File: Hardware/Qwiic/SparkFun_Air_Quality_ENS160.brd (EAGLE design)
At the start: 25.4 x 25.4 mm, 49 parts, among them J1 QWIIC_RIGHT_ANGLE, J2 QWIIC_RIGHT_ANGLE, U1 AP2127K-1.8V

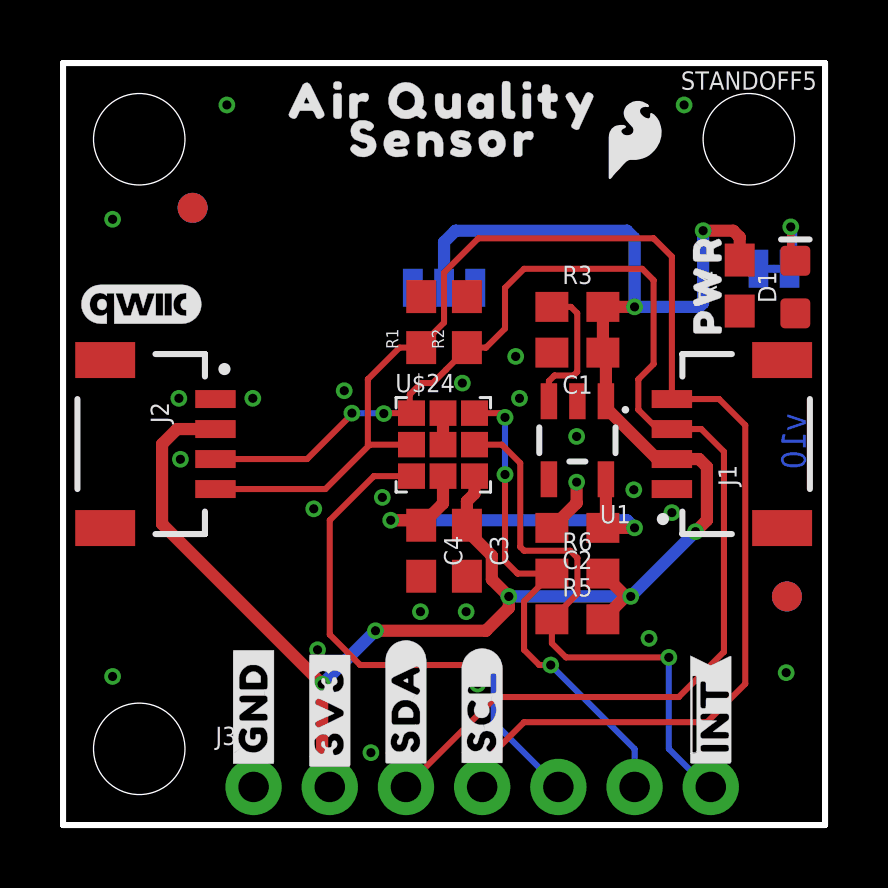
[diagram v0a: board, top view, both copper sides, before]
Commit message: Finishes routing, adds silk
* Updates ENS160 symbol to be smaller
* Adds "U" prefix to device
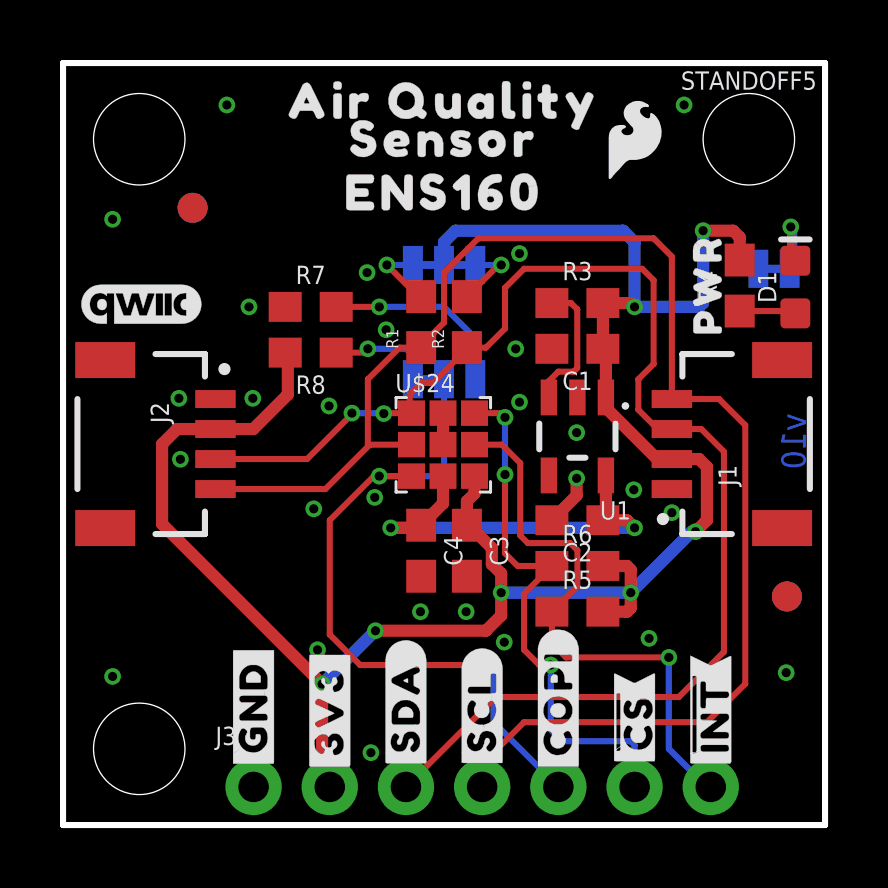
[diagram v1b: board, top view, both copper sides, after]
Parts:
- removed LOGO1: SPECIAL_INSTRUCTIONS-PRODUCTION, SparkFun-Aesthetics:PRODUCTION_INSTRUCTIONS
- added ADDR: JUMPER-SMT_3_1-NC_TRACE_SILK, SparkFun-Jumpers:SMT-JUMPER_3_1-NC_TRACE_SILK
- added R7, R8: 100k, SparkFun-Resistors:0603
- added U$14: (no value), top:#0X53#16019
- added U$15: (no value), top:#0X52#16019
- added U$23: (no value), top:#COPI#16020
- added U$26: (no value), bot:#COPI#441017
- added U$27: (no value), bot:##CS##441016
- added U$28, U$5: (no value), top:ENS16016
- added U$6: (no value), top:#ADDR#6
- U$22: device top:I2C_ADDRESS#441017 -> top:##CS##16019
- U$7: device bot:#SCL#6 -> top:#SCLK#16021
- moved U$22 8.36 mm to (19.1, 3.43), turned to 270 degrees
- moved LOGO3 2.42 mm to (12.7, 8.71)
- moved I2C_PU 0.76 mm to (12.7, 18.7)
- moved U$25 0.52 mm to (12.7, 17.1)
- moved U$7 0.51 mm to (14.0, 4.32)
- moved R5 0.25 mm to (17.1, 7.11)
- moved C2 0.25 mm to (17.1, 10.2)
- moved R6 0.25 mm to (17.1, 8.64)
- moved R3 0.13 mm to (17.1, 17.4)
- moved C1 0.13 mm to (17.1, 15.9)
- moved U1 0.13 mm to (17.1, 13.0)
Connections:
- new net N$4: ADDR.3, R8.1
- new net N$7: ADDR.1, R7.2
- net 3.3V: now also R8.2
- net COPI/ADDR: now also ADDR.2
- net GND: now also R7.1
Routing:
- net N$7: track 0.00 -> 6.44 mm, vias 0 -> 1
- net COPI/ADDR: track 18.0 -> 23.2 mm, vias 1 -> 2
- net 3.3V: track 66.0 -> 70.3 mm
- net N$4: track 0.00 -> 3.49 mm, vias 0 -> 1
- net N$6: track 0.00 -> 2.44 mm, vias 0 -> 1
- net N$5: track 0.00 -> 2.44 mm, vias 0 -> 1
- net N$2: track 0.11 -> 1.89 mm
- net !CS!: track 17.0 -> 18.2 mm
- net GND: track 2.92 -> 2.79 mm, vias 24 -> 27
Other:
- board text removed: "No Clean Assembly"

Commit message: Fixes ENS160 symbol to use the correct SPI terminology
* Fixes net names that also used the wrong SPI terminology
* Puts pin one symbol on the correct layer for the ENS160
* Generally fixes ground pour in a number of areas
* Changes version number in schematic
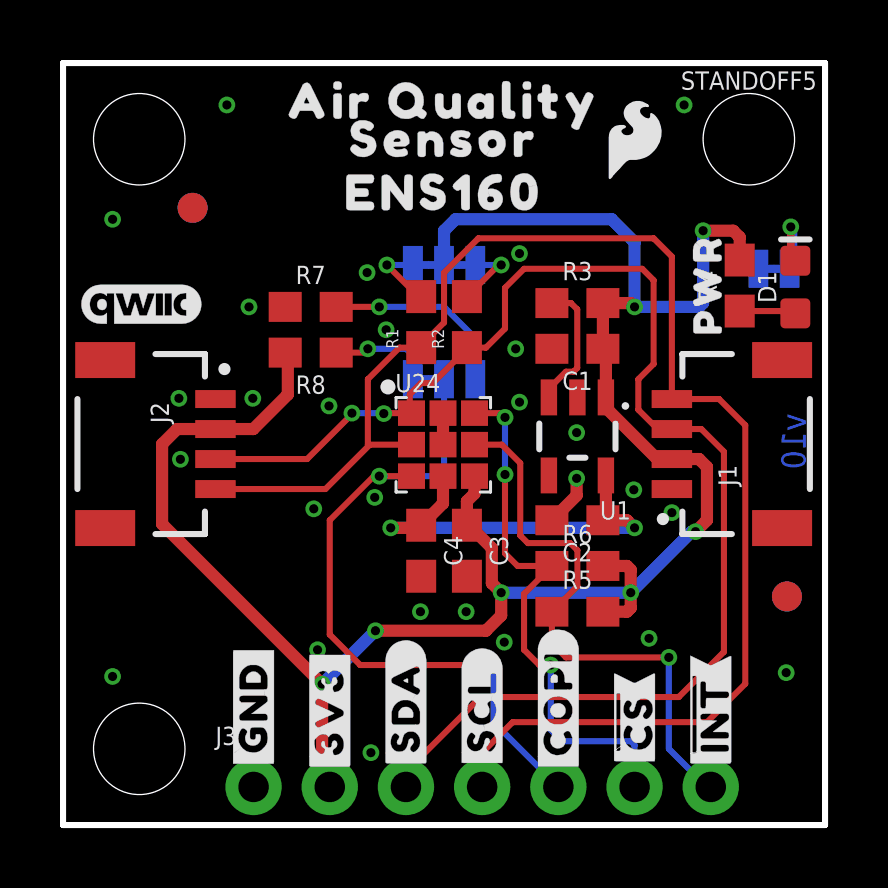
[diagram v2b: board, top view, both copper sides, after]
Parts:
- renumbered U$24 to U24
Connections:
- net CIPO/SDA renamed POCI/SDA
- net COPI/ADDR renamed PICO/ADDR
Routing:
- net 3.3V: track 70.3 -> 70.9 mm
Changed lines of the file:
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@@
 <element name="LOGO4" library="SparkFun-Aesthetics" package="QWIIC_4MM" value="QWIIC_LOGO_4MM" x="2.6162" y="17.3482" smashed="yes"/>
 <element name="U$21" library="top" package="PWR9" value="" x="21.4884" y="18.0086" smashed="yes" rot="R90"/>
-<element name="U$24" library="ENS160" package="LGA-9" value="ENS-160" x="12.7" y="12.7" smashed="yes">
+<element name="U24" library="ENS160" package="LGA-9" value="ENS-160" x="12.7" y="12.7" smashed="yes">
 <attribute name="NAME" x="11.0744" y="14.4272" size="0.6096" layer="25" font="vector" ratio="20"/>
 <attribute name="PROD_ID" value="IC-17100" x="12.7" y="12.7" size="1.778" layer="27" display="off"/>
@@
 <contactref element="U1" pad="2"/>
 <contactref element="C2" pad="2"/>
-<contactref element="U$24" pad="P8"/>
-<contactref element="U$24" pad="P9"/>
+<contactref element="U24" pad="P8"/>
+<contactref element="U24" pad="P9"/>
 <contactref element="J3" pad="1"/>
 <contactref element="C3" pad="2"/>
@@
 <contactref element="U1" pad="1"/>
 <contactref element="R3" pad="2"/>
-<contactref element="U$24" pad="P5"/>
+<contactref element="U24" pad="P5"/>
 <contactref element="R5" pad="2"/>
 <contactref element="R6" pad="2"/>
@@
 <wire x1="20.955" y1="9.779" x2="18.923" y2="7.747" width="0.4064" layer="16"/>
 <via x="14.605" y="7.747" extent="1-16" drill="0.3048"/>
-<wire x1="14.605" y1="7.747" x2="14.605" y2="8.382" width="0.4064" layer="1"/>
-<wire x1="14.605" y1="8.382" x2="14.2922" y2="8.6948" width="0.4064" layer="1"/>
-<wire x1="14.2922" y1="8.6948" x2="14.2922" y2="9.234775" width="0.4064" layer="1"/>
+<wire x1="14.605" y1="7.747" x2="14.2922" y2="8.0598" width="0.4064" layer="1"/>
+<wire x1="14.2922" y1="8.0598" x2="14.2922" y2="9.234775" width="0.4064" layer="1"/>
 <wire x1="13.462" y1="9.994" x2="13.532975" y2="9.994" width="0.4064" layer="1"/>
 <wire x1="14.2922" y1="9.234775" x2="13.532975" y2="9.994" width="0.4064" layer="1"/>
@@
 <wire x1="22.5552" y1="19.5952" x2="22.5552" y2="18.8332" width="0.4064" layer="1"/>
 <wire x1="21.209" y1="17.272" x2="21.336" y2="17.399" width="0.4064" layer="16"/>
-<wire x1="12.7" y1="18.669" x2="12.7" y2="19.431" width="0.4064" layer="16"/>
-<wire x1="18.669" y1="19.812" x2="19.05" y2="19.431" width="0.4064" layer="16"/>
+<wire x1="12.7" y1="18.669" x2="12.7" y2="19.812" width="0.4064" layer="16"/>
+<wire x1="18.288" y1="20.193" x2="19.05" y2="19.431" width="0.4064" layer="16"/>
 <wire x1="19.05" y1="19.431" x2="19.05" y2="17.272" width="0.4064" layer="16"/>
-<wire x1="12.7" y1="19.431" x2="13.081" y2="19.812" width="0.4064" layer="16"/>
-<wire x1="13.081" y1="19.812" x2="18.669" y2="19.812" width="0.4064" layer="16"/>
+<wire x1="12.7" y1="19.812" x2="13.081" y2="20.193" width="0.4064" layer="16"/>
+<wire x1="13.081" y1="20.193" x2="18.288" y2="20.193" width="0.4064" layer="16"/>
 <wire x1="18.923" y1="7.747" x2="14.605" y2="7.747" width="0.4064" layer="16"/>
 <via x="18.923" y="7.747" extent="1-16" drill="0.3048"/>
@@
 </signal>
 <signal name="!INT!">
-<contactref element="U$24" pad="P6"/>
+<contactref element="U24" pad="P6"/>
 <contactref element="R5" pad="1"/>
 <contactref element="J3" pad="7"/>
@@
 <contactref element="U1" pad="5"/>
 <contactref element="C2" pad="1"/>
-<contactref element="U$24" pad="P4"/>
+<contactref element="U24" pad="P4"/>
 <contactref element="C4" pad="1"/>
 <wire x1="18.095" y1="10.260003125" x2="17.995" y2="10.16" width="0.4064" layer="1"/>
@@
 <contactref element="U1" pad="3"/>
 <contactref element="R3" pad="1"/>
-<wire x1="16.195" y1="14.2541" x2="16.195" y2="14.798" width="0.2032" layer="1"/>
-<wire x1="16.195" y1="14.798" x2="16.51" y2="15.113" width="0.2032" layer="1"/>
-<wire x1="16.51" y1="15.113" x2="17.018" y2="15.113" width="0.2032" layer="1"/>
+<wire x1="16.195" y1="14.2541" x2="16.195" y2="14.544" width="0.2032" layer="1"/>
+<wire x1="16.195" y1="14.544" x2="16.764" y2="15.113" width="0.2032" layer="1"/>
+<wire x1="16.764" y1="15.113" x2="17.018" y2="15.113" width="0.2032" layer="1"/>
 <wire x1="17.018" y1="15.113" x2="17.1402" y2="15.2352" width="0.2032" layer="1"/>
 <wire x1="17.1402" y1="17.1888" x2="16.93" y2="17.399" width="0.2032" layer="1"/>
@@
 <wire x1="17.1402" y1="15.2352" x2="17.1402" y2="17.1888" width="0.2032" layer="1"/>
 </signal>
-<signal name="COPI/ADDR">
-<contactref element="U$24" pad="P3"/>
+<signal name="PICO/ADDR">
+<contactref element="U24" pad="P3"/>
 <contactref element="J3" pad="5"/>
 <via x="14.351" y="5.334" extent="1-16" drill="0.3048"/>
@@
 </signal>
 <signal name="SCLK/SCL">
-<contactref element="U$24" pad="P2"/>
+<contactref element="U24" pad="P2"/>
 <contactref element="J1" pad="4"/>
 <contactref element="R1" pad="1"/>
@@
 <wire x1="11.938" y1="15.914" x2="11.938" y2="15.9867125" width="0.2032" layer="1"/>
 <wire x1="12.7" y1="16.7487125" x2="12.7" y2="18.415" width="0.2032" layer="1"/>
-<wire x1="12.7" y1="18.415" x2="13.0175" y2="18.7325" width="0.2032" layer="1"/>
-<wire x1="13.0175" y1="18.7325" x2="13.843" y2="19.558" width="0.2032" layer="1"/>
+<wire x1="12.7" y1="18.415" x2="13.843" y2="19.558" width="0.2032" layer="1"/>
 <wire x1="20.2946" y1="18.9484" x2="20.2946" y2="14.2" width="0.2032" layer="1"/>
 <wire x1="13.843" y1="19.558" x2="19.685" y2="19.558" width="0.2032" layer="1"/>
@@
 <wire x1="21.868" y1="14.2" x2="22.741" y2="13.327" width="0.2032" layer="1"/>
 <wire x1="22.741" y1="4.707" x2="21.463" y2="3.429" width="0.2032" layer="1"/>
-<wire x1="21.463" y1="3.429" x2="15.367" y2="3.429" width="0.2032" layer="1"/>
-<wire x1="13.97" y1="2.032" x2="15.367" y2="3.429" width="0.2032" layer="1"/>
-<wire x1="13.97" y1="1.27" x2="13.97" y2="2.032" width="0.2032" layer="1"/>
-</signal>
-<signal name="CIPO/SDA">
-<contactref element="U$24" pad="P1"/>
+<wire x1="21.463" y1="3.429" x2="14.986" y2="3.429" width="0.2032" layer="1"/>
+<wire x1="14.986" y1="3.429" x2="13.97" y2="2.413" width="0.2032" layer="1"/>
+<wire x1="13.97" y1="1.27" x2="13.97" y2="2.413" width="0.2032" layer="1"/>
+</signal>
+<signal name="POCI/SDA">
+<contactref element="U24" pad="P1"/>
 <contactref element="J1" pad="3"/>
 <contactref element="R2" pad="1"/>
@@
 <wire x1="22.0298" y1="12.446" x2="22.0298" y2="5.7738" width="0.2032" layer="1"/>
 <wire x1="22.0298" y1="5.7738" x2="20.5232" y2="4.2672" width="0.2032" layer="1"/>
-<wire x1="20.5232" y1="4.2672" x2="14.4272" y2="4.2672" width="0.2032" layer="1"/>
-<wire x1="11.43" y1="1.27" x2="14.4272" y2="4.2672" width="0.2032" layer="1"/>
+<wire x1="20.5232" y1="4.2672" x2="13.9192" y2="4.2672" width="0.2032" layer="1"/>
+<wire x1="11.43" y1="1.27" x2="11.43" y2="1.778" width="0.2032" layer="1"/>
+<wire x1="13.9192" y1="4.2672" x2="11.43" y2="1.778" width="0.2032" layer="1"/>
 <wire x1="20.2946" y1="13.2" x2="21.2758" y2="13.2" width="0.2032" layer="1"/>
 <wire x1="21.2758" y1="13.2" x2="22.0298" y2="12.446" width="0.2032" layer="1"/>
 <wire x1="13.462" y1="15.914" x2="13.462" y2="15.875" width="0.2032" layer="1"/>
-<wire x1="13.462" y1="15.875" x2="12.7635" y2="15.1765" width="0.2032" layer="1"/>
-<wire x1="12.7635" y1="15.1765" x2="12.319" y2="14.732" width="0.2032" layer="1"/>
+<wire x1="13.462" y1="15.875" x2="12.319" y2="14.732" width="0.2032" layer="1"/>
 </signal>
 <signal name="!CS!">
-<contactref element="U$24" pad="P7"/>
+<contactref element="U24" pad="P7"/>
 <contactref element="R6" pad="1"/>
 <contactref element="J3" pad="6"/>

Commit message: Updates board to reflect changes in pin numbers
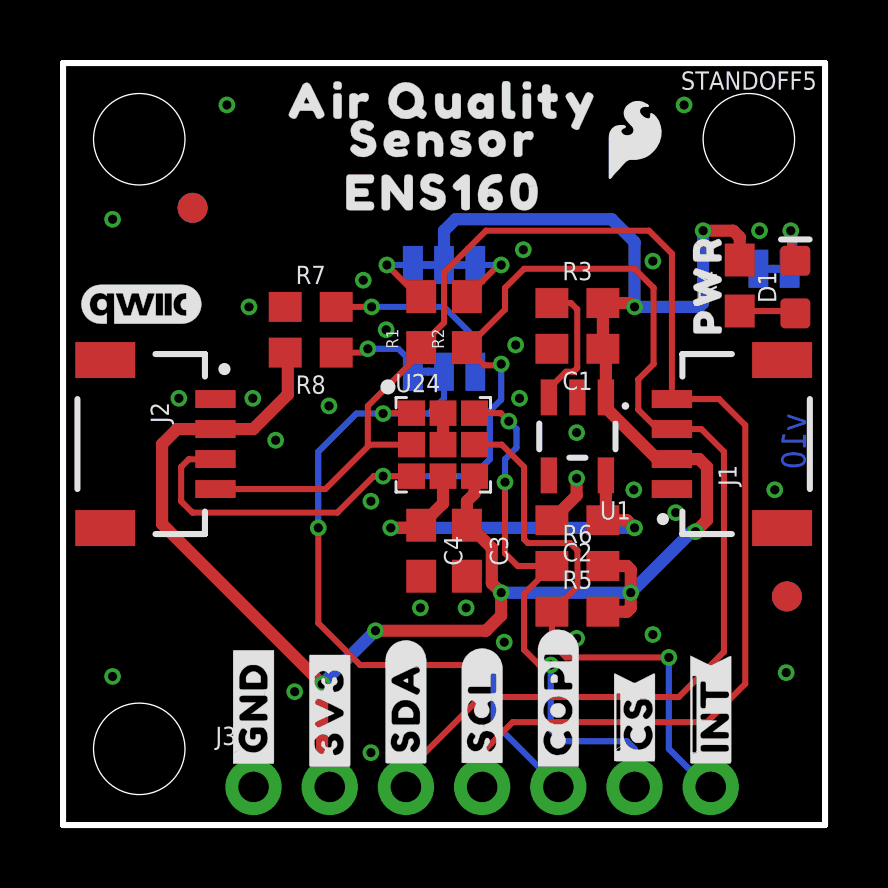
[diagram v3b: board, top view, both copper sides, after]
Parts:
- moved ADDR 0.25 mm to (12.7, 15.1)
- moved U$14 0.25 mm to (9.40, 15.1)
- moved U$15 0.25 mm to (16.0, 15.1)
- moved U$6 0.25 mm to (12.7, 13.6)
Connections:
- net PICO/ADDR: now also U24.P1; no longer U24.P3
- net POCI/SDA: now also U24.P3; no longer U24.P1
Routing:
- net POCI/SDA: track 46.1 -> 54.4 mm
- net PICO/ADDR: track 23.2 -> 23.9 mm, vias 2 -> 3
- net GND: vias 27 -> 30

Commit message: Updated decoupling cap on VDD
* Updates silk
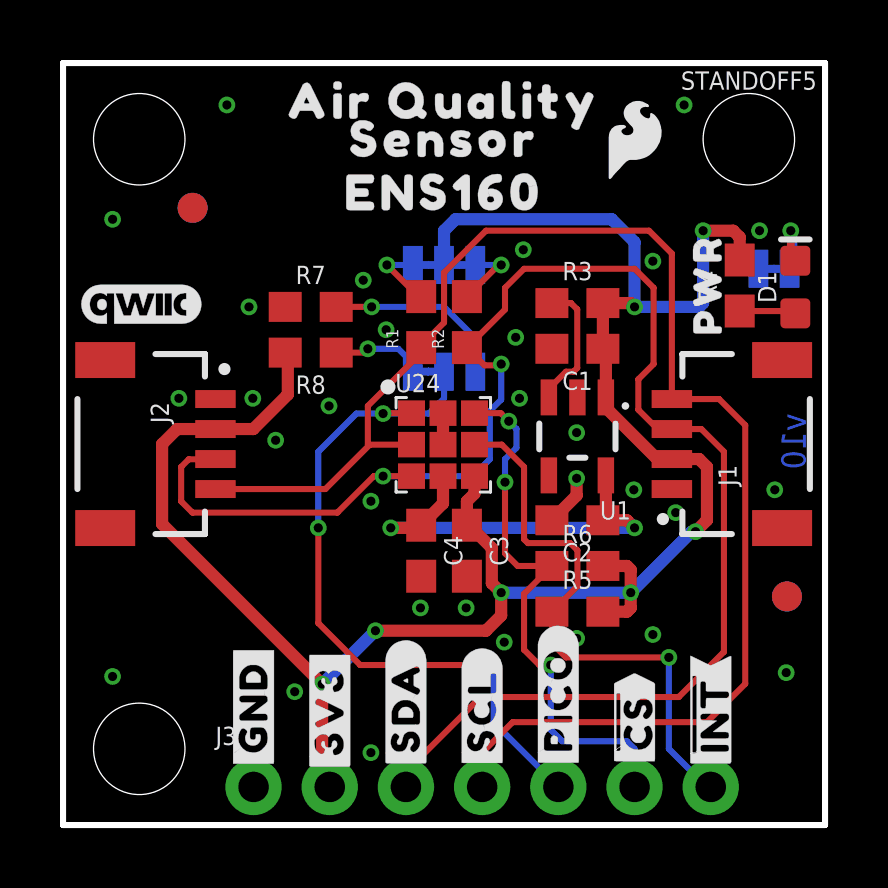
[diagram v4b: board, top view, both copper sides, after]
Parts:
- removed U$27: (no value), bot:##CS##441016
- added U$24: (no value), top:#PICO#16021
- C4: value 0.1uF -> 10uF
- U$22: device top:##CS##16019 -> bot:##CS##441016
- U$23: device top:#COPI#16020 -> top:##CS##16019
- U$26: device bot:#COPI#441017 -> top:#POCI#16020
- U$8: device bot:#SDA#7 -> bot:#PICO#441017
- moved U$8 5.09 mm to (16.5, 4.19), flipped to the top, turned to 90 degrees
- moved U$26 5.08 mm to (11.4, 4.19), flipped to the bottom, turned to 270 degrees
- moved U$23 2.65 mm to (19.1, 3.43)
- flipped U$22 to the top, turned to 90 degrees
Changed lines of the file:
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@@
 <element name="U$3" library="top" package="#SDA#5" value="" x="11.43" y="3.937" smashed="yes" rot="R90"/>
 <element name="U$4" library="top" package="#SCL#4" value="" x="13.97" y="3.81" smashed="yes" rot="R90"/>
-<element name="U$8" library="bot" package="#SDA#7" value="" x="11.43" y="3.937" smashed="yes" rot="MR270"/>
 <element name="U$9" library="top" package="#GND#3" value="" x="6.35" y="3.937" smashed="yes" rot="MR270"/>
 <element name="U$10" library="top" package="#3V3#4" value="" x="8.89" y="3.81" smashed="yes" rot="MR270"/>
@@
 <attribute name="VALUE" x="12.7" y="9.144" size="0.6096" layer="27" font="vector" ratio="20" rot="R270" align="top-center"/>
 </element>
-<element name="C4" library="SparkFun-Capacitors" package="0603" value="0.1uF" x="11.938" y="9.144" smashed="yes" rot="R270">
+<element name="C4" library="SparkFun-Capacitors" package="0603" value="10uF" x="11.938" y="9.144" smashed="yes" rot="R270">
 <attribute name="NAME" x="12.7" y="9.144" size="0.6096" layer="25" font="vector" ratio="20" rot="R270" align="bottom-center"/>
-<attribute name="PROD_ID" value="CAP-00810" x="11.938" y="9.144" size="1.778" layer="27" rot="R270" display="off"/>
-<attribute name="VALUE" x="11.176" y="9.144" size="0.6096" layer="27" font="vector" ratio="20" rot="R270" align="top-center"/>
+<attribute name="PROD_ID" value="CAP-11015" x="11.938" y="9.144" size="1.778" layer="27" rot="R270" display="off"/>
+<attribute name="VALUE" value="10uF" x="11.176" y="9.144" size="0.6096" layer="27" font="vector" ratio="20" rot="R270" align="top-center"/>
 </element>
 <element name="ADDR" library="SparkFun-Jumpers" package="SMT-JUMPER_3_1-NC_TRACE_SILK" package3d_urn="urn:adsk.eagle:package:39288/1" value="JUMPER-SMT_3_1-NC_TRACE_SILK" x="12.7" y="15.113" smashed="yes" rot="MR0">
@@
 <element name="U$14" library="top" package="#0X53#16019" value="" x="9.398" y="15.113" smashed="yes" rot="MR0"/>
 <element name="U$15" library="top" package="#0X52#16019" value="" x="16.002" y="15.113" smashed="yes" rot="MR0"/>
-<element name="U$22" library="top" package="##CS##16019" value="" x="19.05" y="3.429" smashed="yes" rot="MR270"/>
-<element name="U$23" library="top" package="#COPI#16020" value="" x="16.51" y="4.191" smashed="yes" rot="MR270"/>
 <element name="U$7" library="top" package="#SCLK#16021" value="" x="13.97" y="4.318" smashed="yes" rot="MR270"/>
-<element name="U$26" library="bot" package="#COPI#441017" value="" x="16.51" y="4.064" smashed="yes" rot="R90"/>
-<element name="U$27" library="bot" package="##CS##441016" value="" x="19.05" y="3.429" smashed="yes" rot="R90"/>
 <element name="U$28" library="top" package="ENS16016" value="" x="12.7" y="21.082" smashed="yes"/>
+<element name="U$8" library="bot" package="#PICO#441017" value="" x="16.51" y="4.191" smashed="yes" rot="R90"/>
+<element name="U$22" library="bot" package="##CS##441016" value="" x="19.05" y="3.429" smashed="yes" rot="R90"/>
+<element name="U$23" library="top" package="##CS##16019" value="" x="19.05" y="3.429" smashed="yes" rot="MR270"/>
+<element name="U$24" library="top" package="#PICO#16021" value="" x="16.51" y="4.191" smashed="yes" rot="MR270"/>
+<element name="U$26" library="top" package="#POCI#16020" value="" x="11.43" y="4.191" smashed="yes" rot="MR270"/>
 </elements>
 <signals>
@@
 <contactref element="C4" pad="2"/>
 <via x="17.1196" y="13.081" extent="1-16" drill="0.3048"/>
-<via x="15.0876" y="16.002" extent="1-16" drill="0.3048"/>
+<via x="15.0876" y="16.256" extent="1-16" drill="0.3048"/>
 <via x="17.1196" y="11.557" extent="1-16" drill="0.3048"/>
 <via x="20.4216" y="10.414" extent="1-16" drill="0.3048"/>
